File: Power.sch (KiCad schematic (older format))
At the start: 0 parts

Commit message: Power Protection & Filtering
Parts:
- added C? (x2): C, ~, symbol C
- added F? (x4): FUSE, ~, symbol FUSE
- added L? (x2): INDUCTOR, ~, symbol INDUCTOR
- added P?: CONN_12X2, symbol CONN_12X2
- added R?: R, ~, symbol R
- added SW?: SWITCH_INV, ~, symbol SWITCH_INV
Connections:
- net labels added: +12P, +12V, +3.3V, +5V, -12P, -12V, GND
- wire segments 0 -> 35

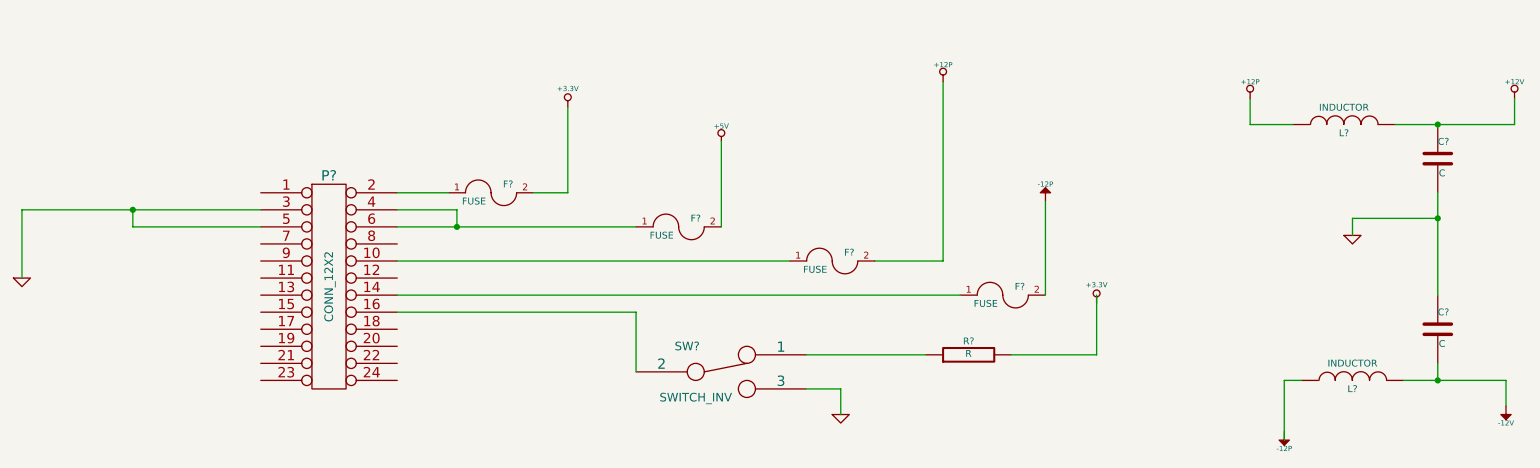
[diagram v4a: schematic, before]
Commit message: Fan/Current Module Refactoring
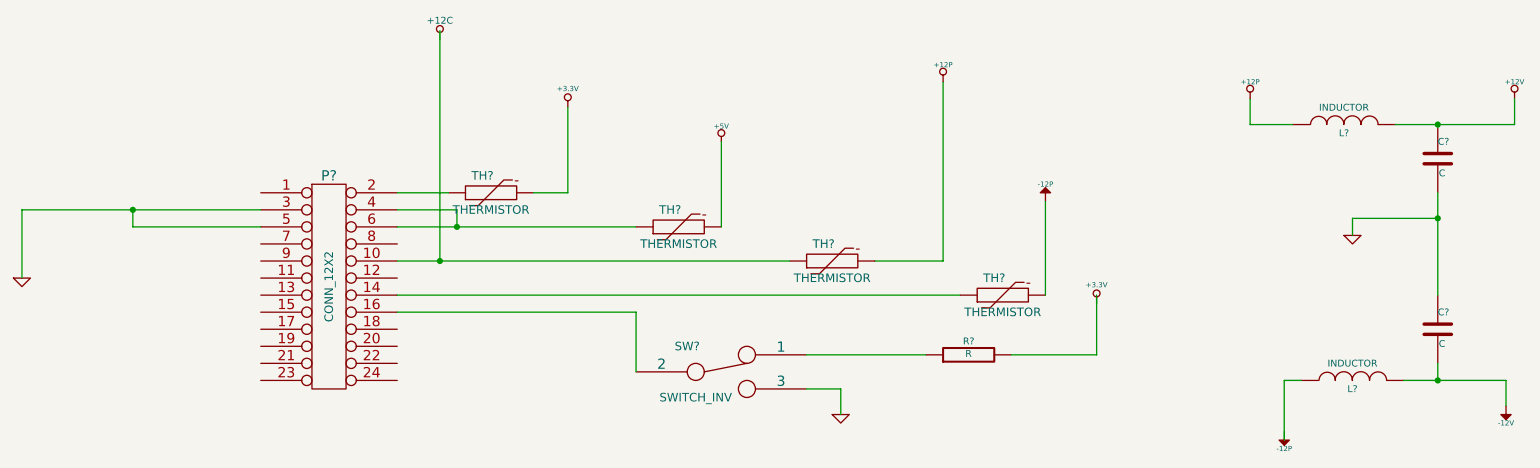
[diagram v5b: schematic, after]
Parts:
- removed F? (x4): FUSE, ~, symbol FUSE
- added TH? (x4): THERMISTOR, ~, symbol THERMISTOR
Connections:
- net labels added: +12C
- wire segments 35 -> 36
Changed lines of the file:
@@
 Sheet 4 9
 Title ""
-Date "24 may 2014"
+Date "25 may 2014"
 Rev ""
 Comp ""
@@
 F 3 "" H 5500 2000 60  0000 C CNN
 	1    5500 2000
-	1    0    0    -1
-$EndComp
-$Comp
-L FUSE F?
-U 1 1 537D7F08
-P 6150 2700
-F 0 "F?" H 6250 2750 40  0000 C CNN
-F 1 "FUSE" H 6050 2650 40  0000 C CNN
-F 2 "~" H 6150 2700 60  0000 C CNN
-F 3 "~" H 6150 2700 60  0000 C CNN
-	1    6150 2700
-	1    0    0    -1
-$EndComp
-$Comp
-L FUSE F?
-U 1 1 537D7F15
-P 5050 2500
-F 0 "F?" H 5150 2550 40  0000 C CNN
-F 1 "FUSE" H 4950 2450 40  0000 C CNN
-F 2 "~" H 5050 2500 60  0000 C CNN
-F 3 "~" H 5050 2500 60  0000 C CNN
-	1    5050 2500
-	1    0    0    -1
-$EndComp
-$Comp
-L FUSE F?
-U 1 1 537D7F1B
-P 7050 2900
-F 0 "F?" H 7150 2950 40  0000 C CNN
-F 1 "FUSE" H 6950 2850 40  0000 C CNN
-F 2 "~" H 7050 2900 60  0000 C CNN
-F 3 "~" H 7050 2900 60  0000 C CNN
-	1    7050 2900
-	1    0    0    -1
-$EndComp
-$Comp
-L FUSE F?
-U 1 1 537D7F21
-P 8050 3100
-F 0 "F?" H 8150 3150 40  0000 C CNN
-F 1 "FUSE" H 7950 3050 40  0000 C CNN
-F 2 "~" H 8050 3100 60  0000 C CNN
-F 3 "~" H 8050 3100 60  0000 C CNN
-	1    8050 3100
 	1    0    0    -1
 $EndComp
@@
 	11050 2100 11050 1950
 Connection ~ 10600 2100
+Wire Wire Line
+	4750 1550 4750 2900
+Connection ~ 4750 2900
+$Comp
+L +12C #PWR?
+U 1 1 53815E81
+P 4750 1600
+F 0 "#PWR?" H 4750 1570 30  0001 C CNN
+F 1 "+12C" H 4750 1710 40  0000 C CNN
+F 2 "" H 4750 1600 60  0000 C CNN
+F 3 "" H 4750 1600 60  0000 C CNN
+	1    4750 1600
+	1    0    0    -1
+$EndComp
+$Comp
+L THERMISTOR TH?
+U 1 1 53816B98
+P 5050 2500
+F 0 "TH?" V 5150 2550 50  0000 C CNN
+F 1 "THERMISTOR" V 4950 2500 50  0000 C CNN
+F 2 "~" H 5050 2500 60  0000 C CNN
+F 3 "~" H 5050 2500 60  0000 C CNN
+	1    5050 2500
+	0    -1   -1   0
+$EndComp
+$Comp
+L THERMISTOR TH?
+U 1 1 53816BA5
+P 6150 2700
+F 0 "TH?" V 6250 2750 50  0000 C CNN
+F 1 "THERMISTOR" V 6050 2700 50  0000 C CNN
+F 2 "~" H 6150 2700 60  0000 C CNN
+F 3 "~" H 6150 2700 60  0000 C CNN
+	1    6150 2700
+	0    -1   -1   0
+$EndComp
+$Comp
+L THERMISTOR TH?
+U 1 1 53816BAB
+P 7050 2900
+F 0 "TH?" V 7150 2950 50  0000 C CNN
+F 1 "THERMISTOR" V 6950 2900 50  0000 C CNN
+F 2 "~" H 7050 2900 60  0000 C CNN
+F 3 "~" H 7050 2900 60  0000 C CNN
+	1    7050 2900
+	0    -1   -1   0
+$EndComp
+$Comp
+L THERMISTOR TH?
+U 1 1 53816BB1
+P 8050 3100
+F 0 "TH?" V 8150 3150 50  0000 C CNN
+F 1 "THERMISTOR" V 7950 3100 50  0000 C CNN
+F 2 "~" H 8050 3100 60  0000 C CNN
+F 3 "~" H 8050 3100 60  0000 C CNN
+	1    8050 3100
+	0    -1   -1   0
+$EndComp
 $EndSCHEMATC
